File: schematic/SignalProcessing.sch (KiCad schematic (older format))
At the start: 2 parts

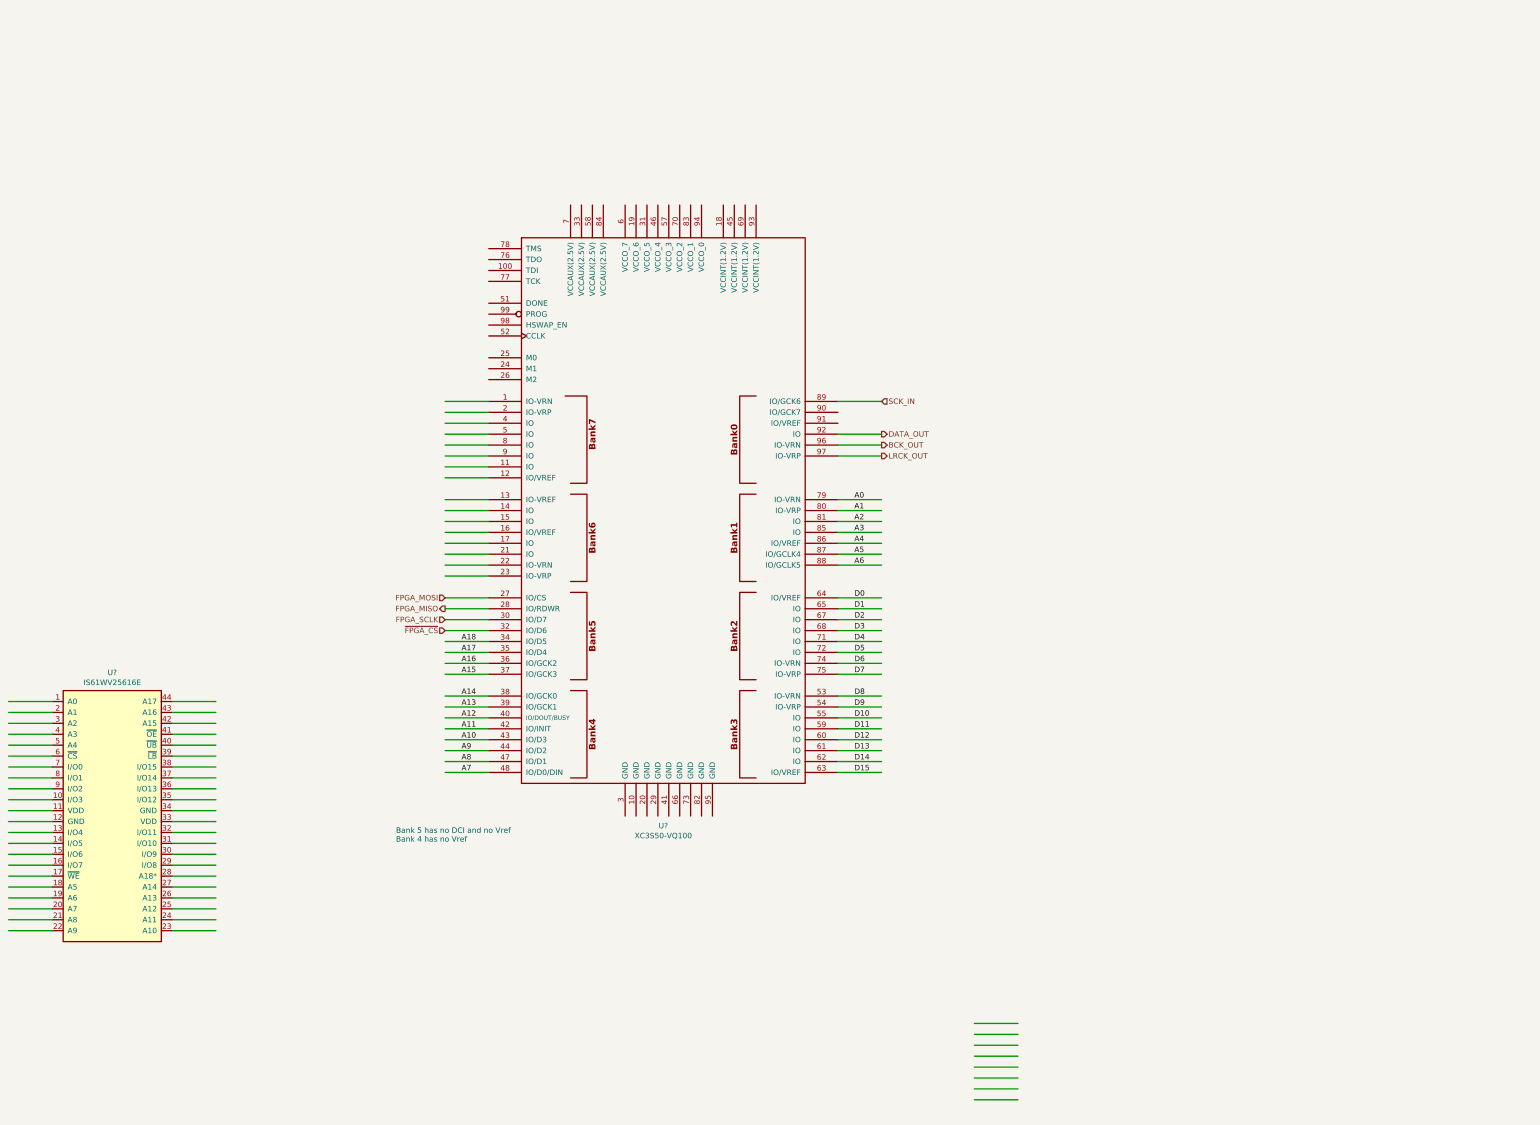
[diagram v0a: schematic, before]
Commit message: Clock generation mostly complete. Some inter-module connections fixed.
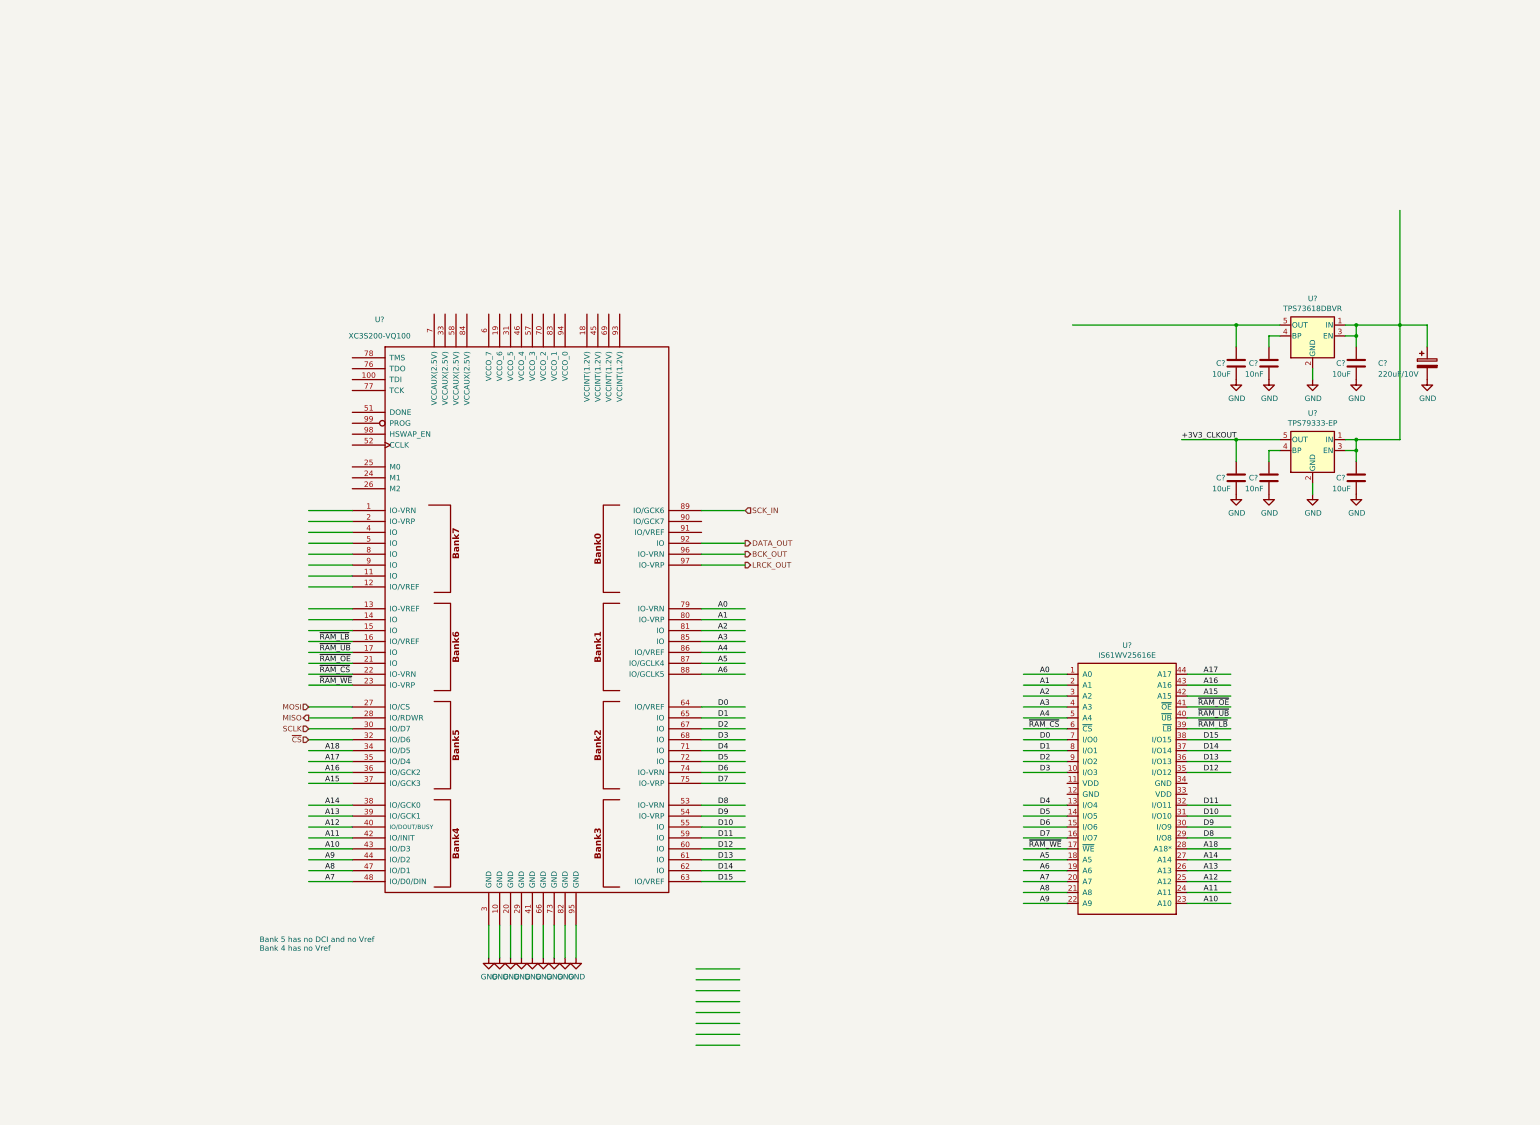
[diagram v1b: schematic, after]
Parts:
- added C? (x2): 10nF, Capacitor_SMD:C_0603_1608Metric, symbol Device:C
- added C? (x4): 10uF, Capacitor_SMD:C_0603_1608Metric, symbol Device:C
- added C?: 220uF/10V, Capacitor_SMD:C_Elec_8x6.2, symbol Device:CP
- added U?: TPS73618DBVR, Package_TO_SOT_SMD:SOT-23-5, symbol Regulator_Linear:TPS79318-EP
- added U?: TPS79333-EP, Package_TO_SOT_SMD:SOT-23-5, symbol Regulator_Linear:TPS79333-EP
- U?: value XC3S50-VQ100 -> XC3S200-VQ100
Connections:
- net labels added: +3V3_CLKOUT, GND, MISO, MOSI, SCLK, ~CS~, ~RAM_CS~, ~RAM_LB~, ~RAM_OE~, ~RAM_UB~, ~RAM_WE~
- net labels removed: FPGA_MISO, FPGA_MOSI, FPGA_SCLK, ~FPGA_CS~
- wire segments 111 -> 142
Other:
- moved on the sheet: U?

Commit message: Remove galvanic isolator - too much jitter! Add USB interface for Debug and program purposes. Swith to Lattice FPGA
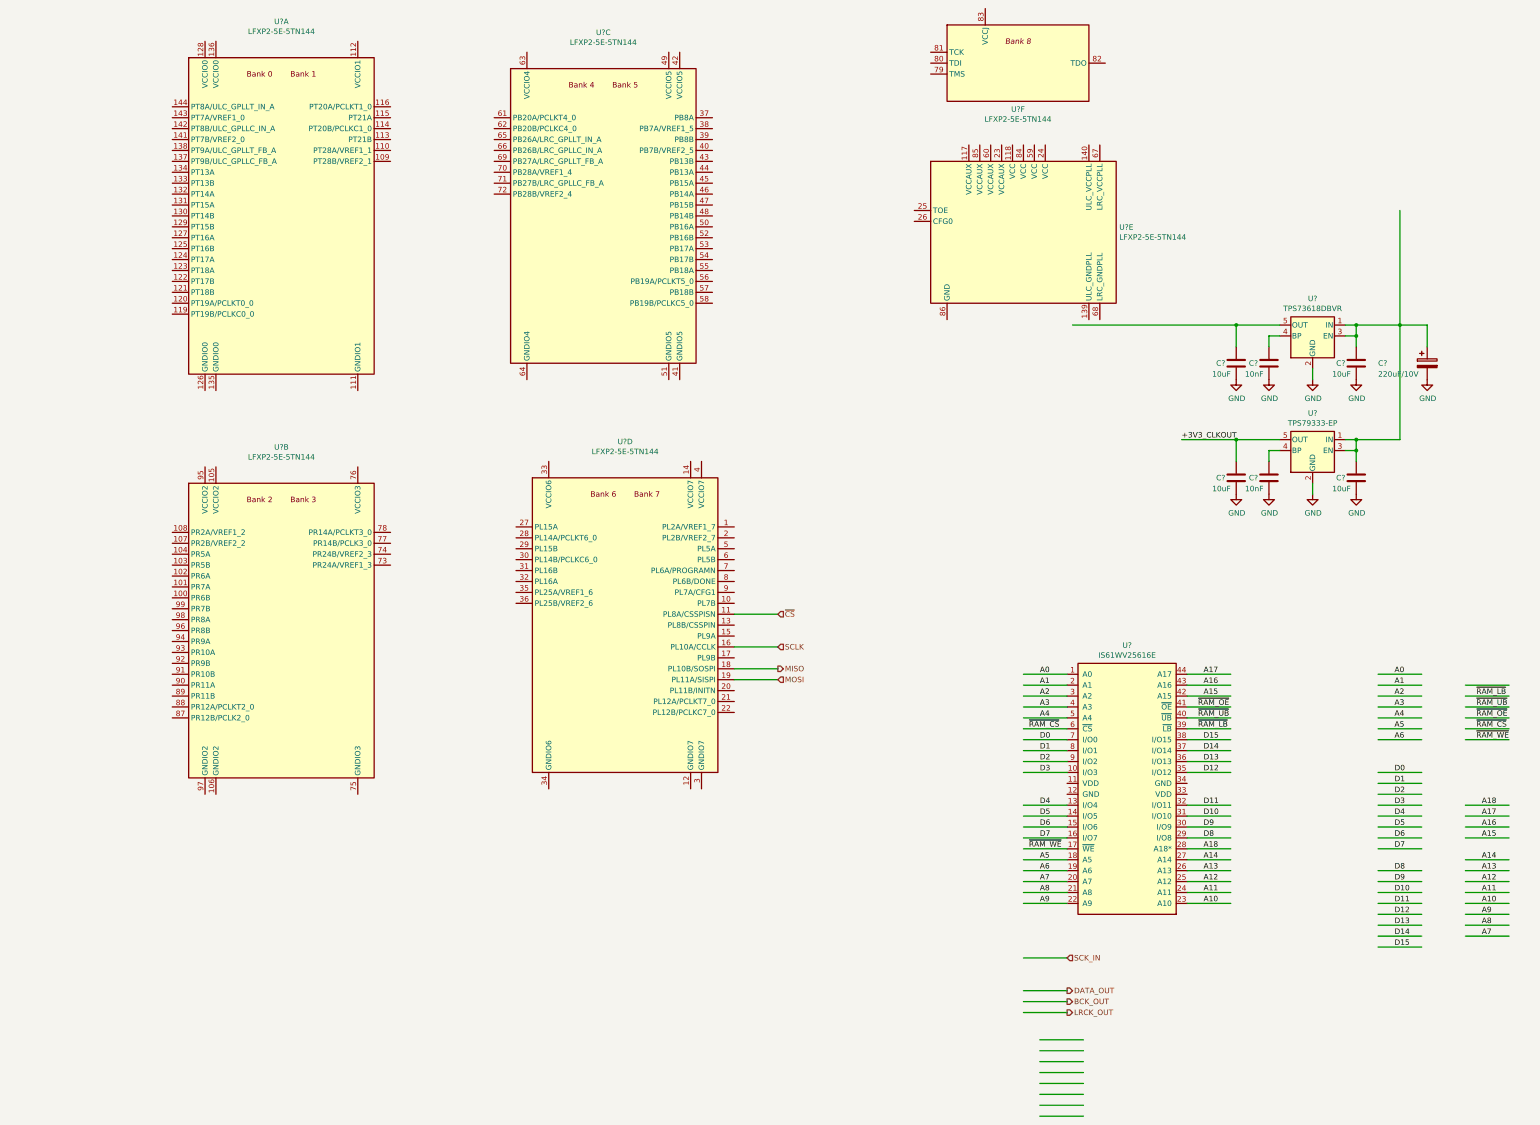
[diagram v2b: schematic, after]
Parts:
- removed U?: XC3S200-VQ100, symbol FPGA_Xilinx:XC3S50-VQ100
- added U? (x6): LFXP2-5E-5TN144, Package_QFP:TQFP-144_20x20mm_P0.5mm, symbol FPGA_Lattice:LFXP2-5E-5TN144
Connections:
- wire segments 142 -> 123
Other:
- note removed: "Bank 5 has no DCI and no Vref\nBank 4 has no Vref"
